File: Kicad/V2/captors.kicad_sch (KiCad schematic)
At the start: 1 part

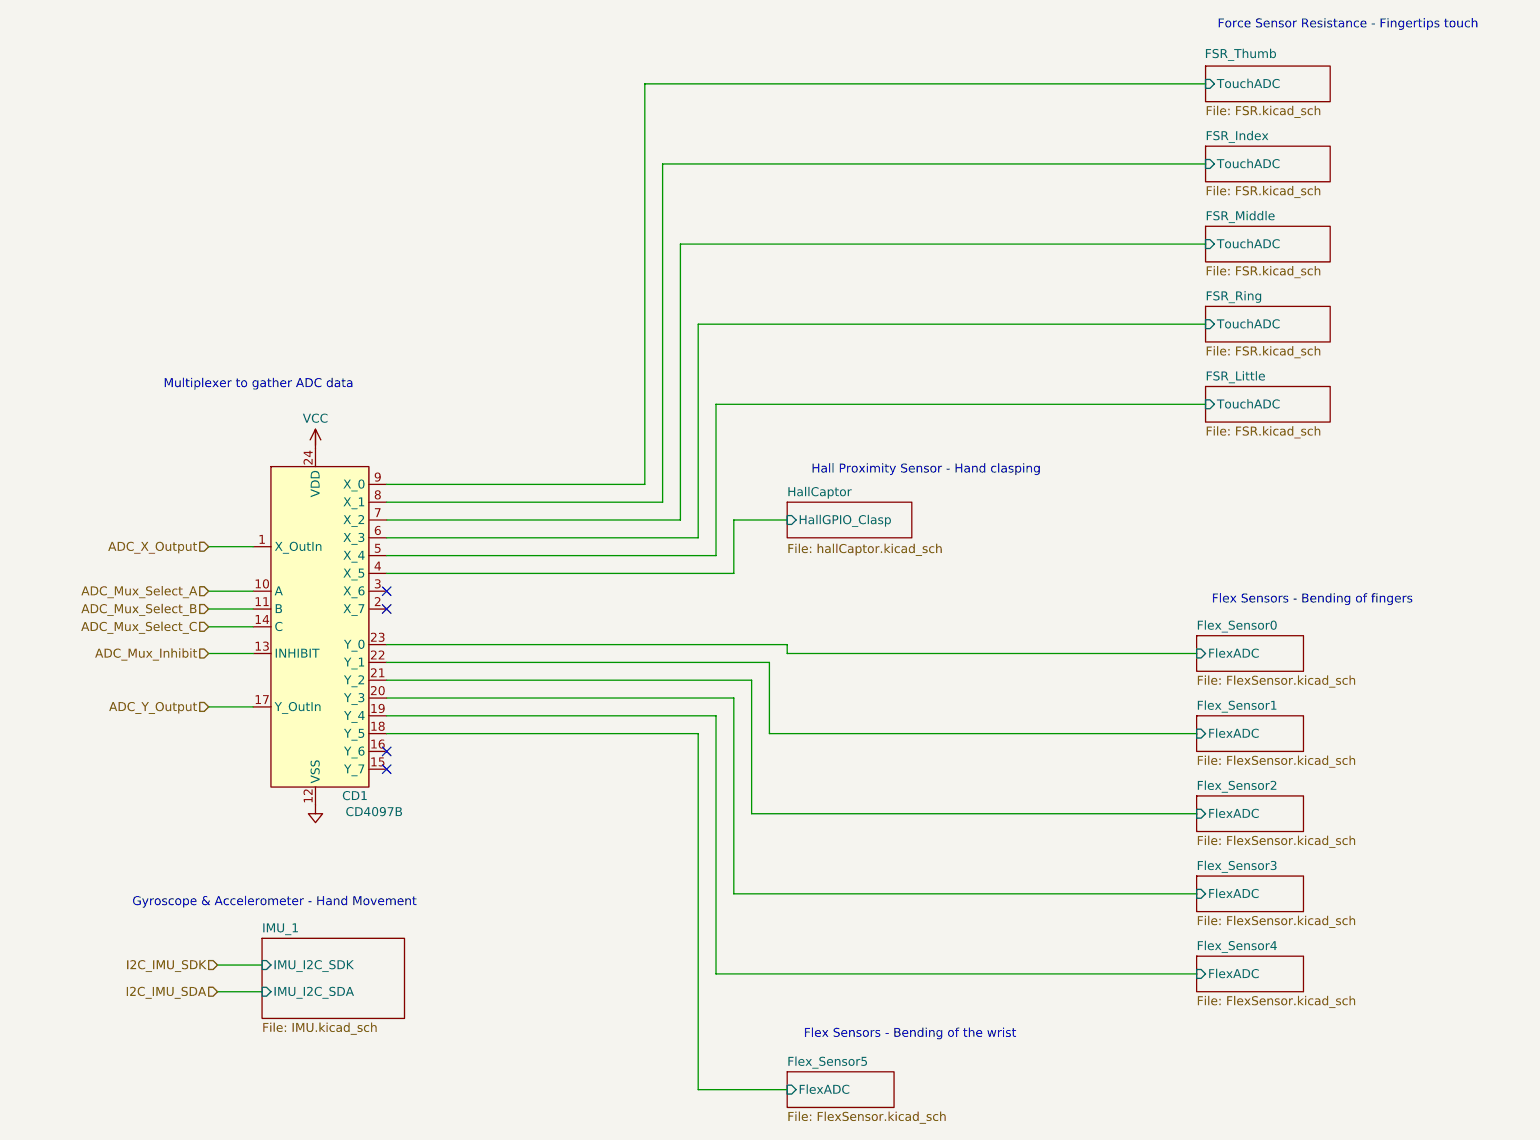
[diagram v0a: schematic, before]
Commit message: correction schema elec + ajout connecteur FPC
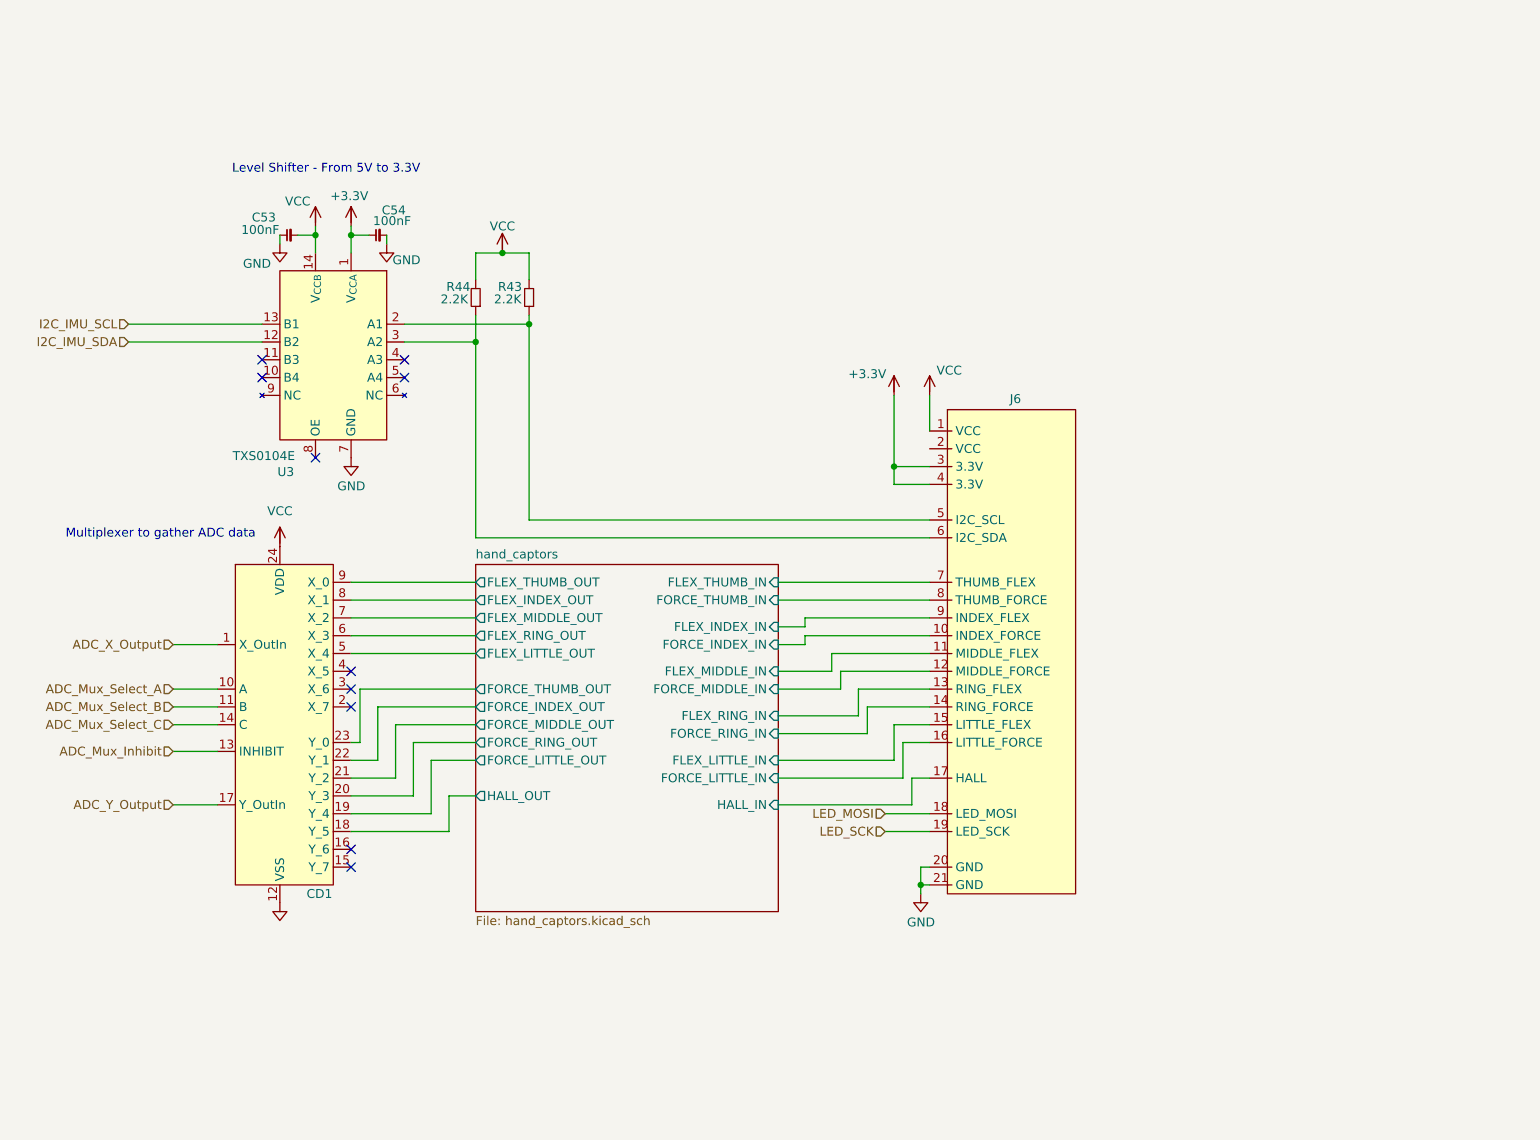
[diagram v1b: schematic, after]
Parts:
- added C53, C54: 100nF, symbol G-Love:C
- added J6: (no value), symbol G-Love:FPC_4_fingers
- added R43, R44: 2.2K, symbol G-Love:R
- added U3: TXS0104E, MyGlove:TXS0104EPWR, symbol G-Love:TXS0104E
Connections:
- net GND: now also C53.2, C54.1, J6.20 (GND), J6.21 (GND), U3.7 (GND)
- net I2C_IMU_SDA: now also U3.12 (B2)
- net VCC: now also C53.1, J6.1 (VCC), R43.2, R44.2, U3.14 (V_{CCB})
- net FSR_Index/TouchADC renamed hand_captors/FLEX_INDEX_OUT
- net FSR_Little/TouchADC renamed hand_captors/FLEX_LITTLE_OUT
- net FSR_Middle/TouchADC renamed hand_captors/FLEX_MIDDLE_OUT
- net FSR_Ring/TouchADC renamed hand_captors/FLEX_RING_OUT
- net FSR_Thumb/TouchADC renamed hand_captors/FLEX_THUMB_OUT
- net Flex_Sensor0/FlexADC renamed hand_captors/FORCE_THUMB_OUT
- net Flex_Sensor1/FlexADC renamed hand_captors/FORCE_INDEX_OUT
- net Flex_Sensor2/FlexADC renamed hand_captors/FORCE_MIDDLE_OUT
- net Flex_Sensor3/FlexADC renamed hand_captors/FORCE_RING_OUT
- net Flex_Sensor4/FlexADC renamed hand_captors/FORCE_LITTLE_OUT
- net Flex_Sensor5/FlexADC renamed hand_captors/HALL_OUT
- net HallCaptor/HallGPIO_Clasp: no longer names the net of CD1.4 (X_5)
- new net: J6.5 (I2C_SCL), R43.1, U3.2 (A1)
- new net: J6.6 (I2C_SDA), R44.1, U3.3 (A2)
- new net +3.3V: C54.2, J6.3 (3.3V), J6.4 (3.3V), U3.1 (V_{CCA})
- new net I2C_IMU_SCL: U3.13 (B1)
- new net LED_MOSI: J6.18 (LED_MOSI)
- new net LED_SCK: J6.19 (LED_SCK)
- new net hand_captors/FLEX_INDEX_IN: J6.9 (INDEX_FLEX)
- new net hand_captors/FLEX_LITTLE_IN: J6.15 (LITTLE_FLEX)
- new net hand_captors/FLEX_MIDDLE_IN: J6.11 (MIDDLE_FLEX)
- new net hand_captors/FLEX_RING_IN: J6.13 (RING_FLEX)
- new net hand_captors/FLEX_THUMB_IN: J6.7 (THUMB_FLEX)
- new net hand_captors/FORCE_INDEX_IN: J6.10 (INDEX_FORCE)
- new net hand_captors/FORCE_LITTLE_IN: J6.16 (LITTLE_FORCE)
- new net hand_captors/FORCE_MIDDLE_IN: J6.12 (MIDDLE_FORCE)
- new net hand_captors/FORCE_RING_IN: J6.14 (RING_FORCE)
- new net hand_captors/FORCE_THUMB_IN: J6.8 (THUMB_FORCE)
- new net hand_captors/HALL_IN: J6.17 (HALL)
- no-connect marks 4 -> 10
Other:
- removed sheet FSR_Index
- removed sheet FSR_Little
- removed sheet FSR_Middle
- removed sheet FSR_Ring
- removed sheet FSR_Thumb
- removed sheet Flex_Sensor0
- removed sheet Flex_Sensor1
- removed sheet Flex_Sensor2
- removed sheet Flex_Sensor3
- removed sheet Flex_Sensor4
- removed sheet Flex_Sensor5
- removed sheet HallCaptor
- removed sheet IMU_1
- added sheet hand_captors (hand_captors.kicad_sch)
- note added: "Level Shifter - From 5V to 3.3V"
- note removed: "Flex Sensors - Bending of fingers"
- note removed: "Flex Sensors - Bending of the wrist"
- note removed: "Force Sensor Resistance - Fingertips touch"
- note removed: "Gyroscope & Accelerometer - Hand Movement"
- note removed: "Hall Proximity Sensor - Hand clasping"
- moved on the sheet: CD1
